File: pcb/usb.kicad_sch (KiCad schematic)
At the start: 40 parts, among them J6 USB4105-GF-A, J7 S2B-PH-SM4-TB, Q1 DMP3099L-7, Q2 DMG3418L, Q3 DMG3418L, SW1 400MSP1R6BLKM6QE, U149 SN74LVC2G132DCUR, U151 AP2112K-3.3, U152 BQ29700DSER, U153 MCP73831T-2ACI/OT

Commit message: Decrease charge indication LED brightness
- 1k current limiting resistor replaced with 4.7k
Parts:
- R283: value 1k -> 4.7k
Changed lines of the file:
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@@
 			)
 		)
-		(property "Value" "1k"
+		(property "Value" "4.7k"
 			(at 210.82 57.15 90)
 			(effects

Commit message: Add light pipe part to schematic.
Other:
- note added: "Light Pipe: PLPC3-125"
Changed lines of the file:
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@@
+		)
+	)
+	(text "Light Pipe: \nPLPC3-125"
+		(exclude_from_sim no)
+		(at 203.2 30.48 0)
+		(effects
+			(font
+				(size 1.27 1.27)
+			)
+			(href "https://www.bivar.com/parts_content/Datasheets/PLPC3-XXX.pdf")
 		)
 	)

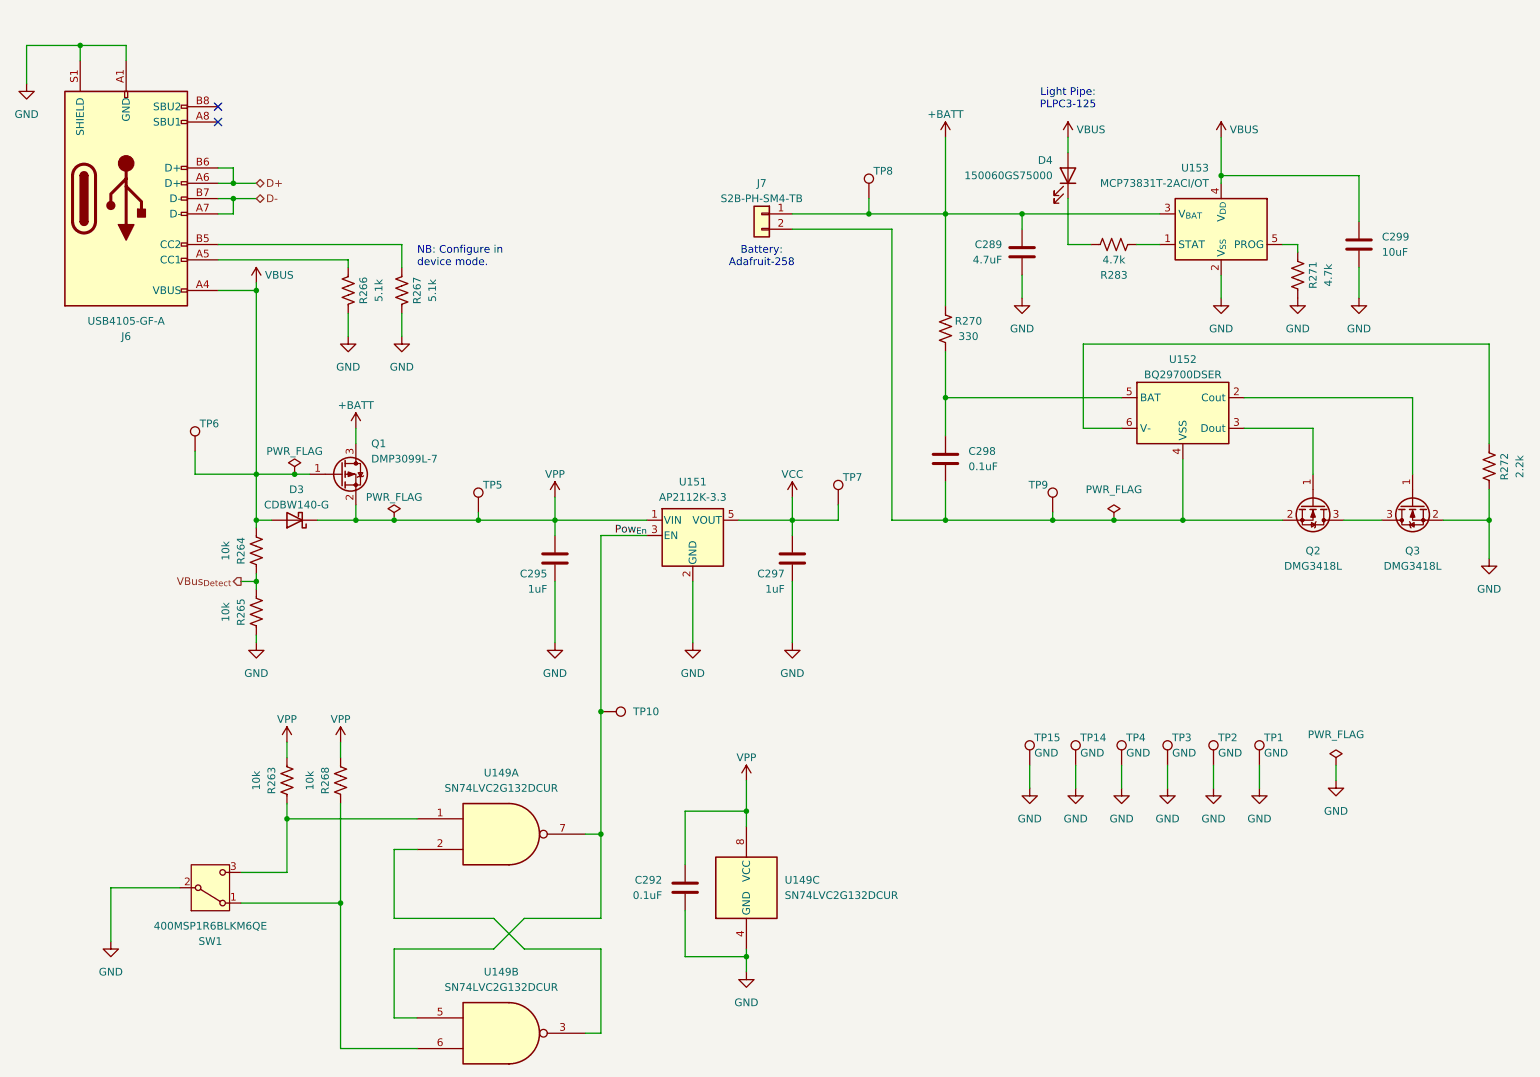
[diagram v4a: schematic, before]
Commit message: Address issues with case found during proptyping
- Add recess for reset button
- Add 3.5V power managment circuit and simplify on/off switch debounce
- Increase space in bottom porition of case for thicker battery
- Remove alignment notches from PCB -- uses features of case instead
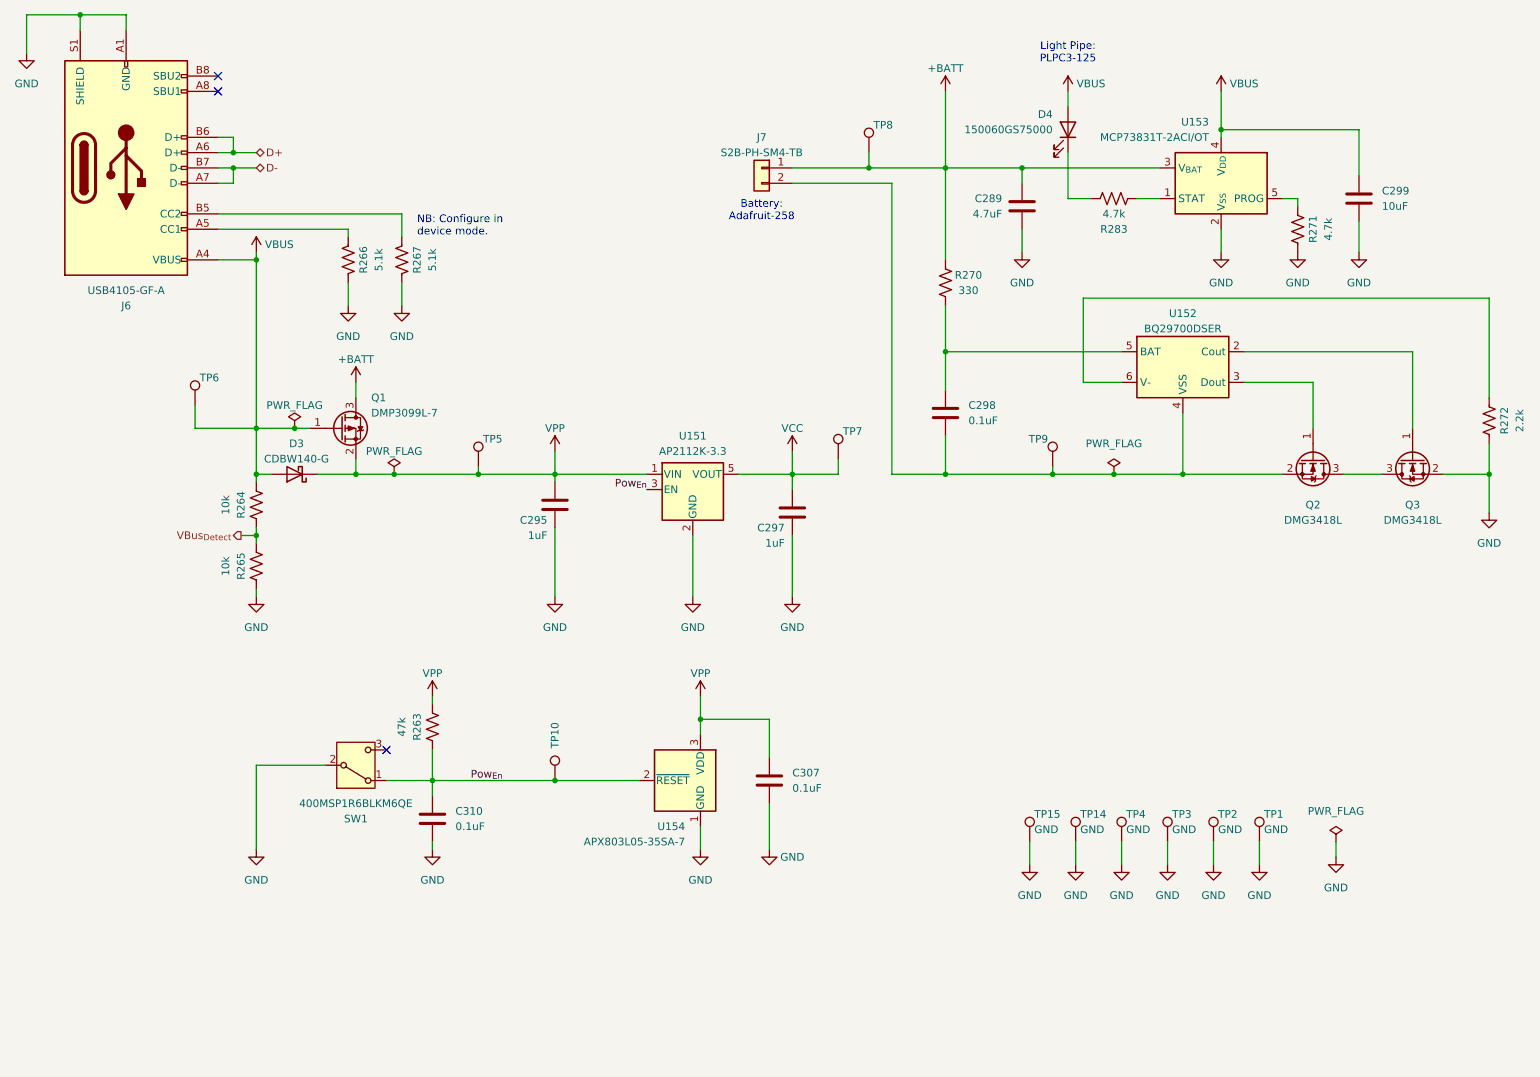
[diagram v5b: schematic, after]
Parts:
- removed C292: 0.1uF, Capacitor_SMD:C_0402_1005Metric, symbol Device:C
- removed R268: 10k, Resistor_SMD:R_0402_1005Metric, symbol Device:R_US
- removed U149: SN74LVC2G132DCUR, Package_SO:VSSOP-8_2.3x2mm_P0.5mm, symbol 74xGxx:74LVC2G00
- added C307, C310: 0.1uF, Capacitor_SMD:C_0402_1005Metric, symbol Device:C
- added U154: APX803L05-35SA-7, Package_TO_SOT_SMD:SOT-23, symbol Power_Supervisor:TPS3839DBZ
- R263: value 10k -> 47k
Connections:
- net GND: now also C307.2, C310.2, U154.1 (GND)
- net Pow_{En}: now also R263.2, SW1.1 (A), C310.1, U154.2 (~{RESET})
- net VPP: now also C307.1, U154.3 (VDD)
- net at SW1.3 (C): no longer R263.2
- no-connect marks 2 -> 3
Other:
- moved on the sheet: C289, C295, C297, C298, C299, D3, D4, J6, J7, Q1, Q2, Q3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

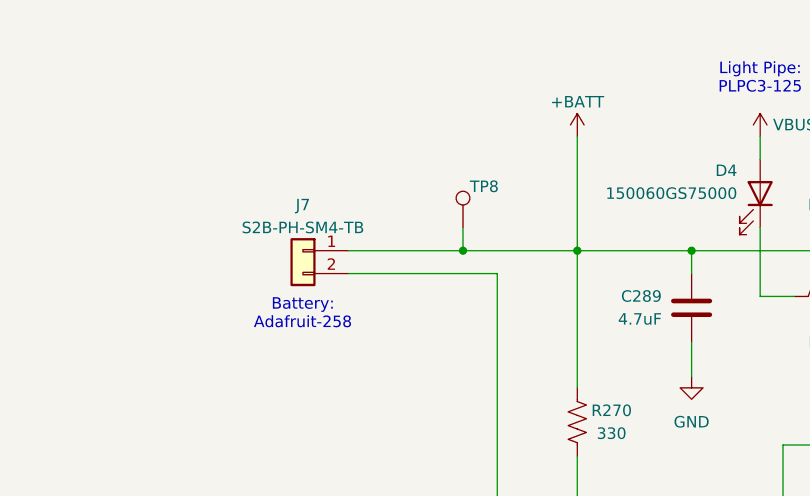
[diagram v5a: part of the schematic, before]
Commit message: Add direct wire to board option for battery
- Original connector is still there, but can be DNP for other battery
  choices.
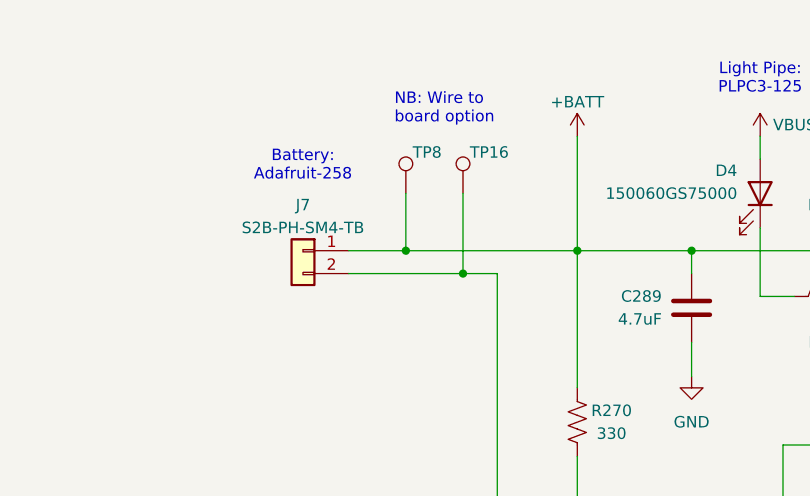
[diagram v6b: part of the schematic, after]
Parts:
- added TP16: ~, TestPoint:TestPoint_THTPad_D3.0mm_Drill1.5mm, symbol Connector:TestPoint
- TP8: value GND -> ~; footprint TestPoint:TestPoint_Pad_D2.0mm -> TestPoint:TestPoint_THTPad_D3.0mm_Drill1.5mm
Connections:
- net at C298.2, J7.2 (Pin_2), Q2.2 (S)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: now also TP16.1
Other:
- note added: "NB: Wire to board option"
- moved on the sheet: TP8
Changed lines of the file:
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@@
 		(comment 1 "Jonathan P. Newman")
 	)
+	(text "NB: Wire to\nboard option"
+		(exclude_from_sim no)
+		(at 162.56 27.94 0)
+		(effects
+			(font
+				(size 1.27 1.27)
+			)
+			(justify left bottom)
+		)
+	)
 	(text "Battery:\nAdafruit-258\n"
 		(exclude_from_sim no)
-		(at 152.4 50.8 0)
+		(at 152.4 34.29 0)
 		(effects
 			(font
@@
 	)
 	(junction
-		(at 182.88 72.39)
+		(at 163.83 41.91)
 		(diameter 0)
 		(color 0 0 0 0)
 	)
 	(junction
-		(at 68.58 102.87)
+		(at 182.88 72.39)
 		(diameter 0)
 		(color 0 0 0 0)
 	)
 	(junction
-		(at 210.82 92.71)
+		(at 68.58 102.87)
 		(diameter 0)
 		(color 0 0 0 0)
 	)
 	(junction
-		(at 157.48 92.71)
+		(at 210.82 92.71)
 		(diameter 0)
 		(color 0 0 0 0)
 	)
 	(junction
-		(at 170.18 41.91)
+		(at 157.48 92.71)
 		(diameter 0)
 		(color 0 0 0 0)
@@
 	)
 	(junction
+		(at 170.18 44.45)
+		(diameter 0)
+		(color 0 0 0 0)
+	)
+	(junction
 		(at 64.77 41.91)
 		(diameter 0)
@@
 	(wire
 		(pts
+			(xy 163.83 41.91) (xy 182.88 41.91)
+		)
+		(stroke
+			(width 0)
+			(type default)
+		)
+	)
+	(wire
+		(pts
 			(xy 212.09 153.67) (xy 212.09 157.48)
 		)
@@
 	(wire
 		(pts
-			(xy 157.48 44.45) (xy 173.99 44.45)
+			(xy 157.48 44.45) (xy 170.18 44.45)
 		)
 		(stroke
@@
 	(wire
 		(pts
+			(xy 170.18 44.45) (xy 173.99 44.45)
+		)
+		(stroke
+			(width 0)
+			(type default)
+		)
+	)
+	(wire
+		(pts
 			(xy 97.79 143.51) (xy 97.79 146.05)
 		)
@@
 	(wire
 		(pts
-			(xy 80.01 140.97) (xy 68.58 140.97)
+			(xy 170.18 35.56) (xy 170.18 44.45)
 		)
 		(stroke
@@
 	(wire
 		(pts
-			(xy 92.71 60.96) (xy 92.71 64.77)
+			(xy 80.01 140.97) (xy 68.58 140.97)
 		)
 		(stroke
@@
 	(wire
 		(pts
-			(xy 228.6 35.56) (xy 228.6 36.83)
+			(xy 92.71 60.96) (xy 92.71 64.77)
 		)
 		(stroke
@@
 	(wire
 		(pts
-			(xy 64.77 41.91) (xy 64.77 44.45)
+			(xy 228.6 35.56) (xy 228.6 36.83)
 		)
 		(stroke
@@
 	(wire
 		(pts
-			(xy 132.08 143.51) (xy 118.11 143.51)
+			(xy 64.77 41.91) (xy 64.77 44.45)
 		)
 		(stroke
@@
 	(wire
 		(pts
-			(xy 62.23 36.83) (xy 64.77 36.83)
+			(xy 132.08 143.51) (xy 118.11 143.51)
 		)
 		(stroke
@@
 	(wire
 		(pts
-			(xy 46.99 16.51) (xy 39.37 16.51)
+			(xy 62.23 36.83) (xy 64.77 36.83)
 		)
 		(stroke
@@
 	(wire
 		(pts
-			(xy 273.05 92.71) (xy 265.43 92.71)
+			(xy 46.99 16.51) (xy 39.37 16.51)
 		)
 		(stroke
@@
 	(wire
 		(pts
-			(xy 170.18 41.91) (xy 182.88 41.91)
+			(xy 273.05 92.71) (xy 265.43 92.71)
 		)
 		(stroke
@@
 	(wire
 		(pts
-			(xy 157.48 41.91) (xy 170.18 41.91)
+			(xy 157.48 41.91) (xy 163.83 41.91)
 		)
 		(stroke
@@
 	(wire
 		(pts
-			(xy 170.18 39.37) (xy 170.18 41.91)
+			(xy 163.83 35.56) (xy 163.83 41.91)
 		)
 		(stroke
@@
 	(symbol
 		(lib_id "Connector:TestPoint")
-		(at 170.18 39.37 0)
+		(at 163.83 35.56 0)
 		(unit 1)
 		(exclude_from_sim no)
@@
 		(dnp no)
 		(property "Reference" "TP8"
-			(at 170.942 34.798 0)
+			(at 164.592 30.988 0)
 			(effects
 				(font
@@
 			)
 		)
-		(property "Value" "GND"
-			(at 170.942 37.338 0)
+		(property "Value" "~"
+			(at 164.592 33.528 0)
 			(effects
 				(font
@@
 			)
 		)
-		(property "Footprint" "TestPoint:TestPoint_Pad_D2.0mm"
-			(at 175.26 39.37 0)
+		(property "Footprint" "TestPoint:TestPoint_THTPad_D3.0mm_Drill1.5mm"
+			(at 168.91 35.56 0)
 			(effects
 				(font
@@
 		)
 		(property "Datasheet" "~"
-			(at 175.26 39.37 0)
+			(at 168.91 35.56 0)
 			(effects
 				(font
@@
 		)
 		(property "Description" "test point"
-			(at 170.18 39.37 0)
+			(at 163.83 35.56 0)
 			(effects
 				(font
@@
 		)
 		(property "Voltage" ""
-			(at 170.18 39.37 0)
+			(at 163.83 35.56 0)
 			(effects
 				(font
@@
 		)
 		(property "Datasheet1" ""
-			(at 170.18 39.37 0)
+			(at 163.83 35.56 0)
 			(effects
 				(font
@@
 		)
 		(property "Part No." ""
-			(at 170.18 39.37 0)
+			(at 163.83 35.56 0)
 			(effects
 				(font
@@
 		)
 		(property "Tolerance" ""
-			(at 170.18 39.37 0)
+			(at 163.83 35.56 0)
 			(effects
 				(font
@@
 					(unit 1)
 				)
+			)
+		)
+	)
+	(symbol
+		(lib_id "Connector:TestPoint")
+		(at 170.18 35.56 0)
+		(unit 1)
+		(exclude_from_sim no)
+		(in_bom yes)
+		(on_board yes)
+		(dnp no)
+		(property "Reference" "TP16"
+			(at 170.942 30.988 0)
+			(effects
+				(font
+					(size 1.27 1.27)
+				)
+				(justify left)
+			)
+		)
+		(property "Value" "~"
+			(at 170.942 33.528 0)
+			(effects
+				(font
+					(size 1.27 1.27)
+				)
+				(justify left)
+				(hide yes)
+			)
+		)
+		(property "Footprint" "TestPoint:TestPoint_THTPad_D3.0mm_Drill1.5mm"
+			(at 175.26 35.56 0)
+			(effects
+				(font
+					(size 1.27 1.27)
+				)
+				(hide yes)
+			)
+		)
+		(property "Datasheet" "~"
+			(at 175.26 35.56 0)
+			(effects
+				(font
+					(size 1.27 1.27)
+				)
+				(hide yes)
+			)
+		)
+		(property "Description" "test point"
+			(at 170.18 35.56 0)
+			(effects
+				(font
+					(size 1.27 1.27)
+				)
+				(hide yes)
+			)
+		)
+		(property "Voltage" ""
+			(at 170.18 35.56 0)
+			(effects
+				(font
+					(size 1.27 1.27)
+				)
+				(hide yes)
+			)
+		)
+		(property "Datasheet1" ""
+			(at 170.18 35.56 0)
+			(effects
+				(font
+					(size 1.27 1.27)
+				)
+				(hide yes)
+			)
+		)
+		(property "Part No." ""
+			(at 170.18 35.56 0)
+			(effects
+				(font
+					(size 1.27 1.27)
+				)
+				(hide yes)
+			)
+		)
+		(property "Tolerance" ""
+			(at 170.18 35.56 0)
+			(effects
+				(font
+					(size 1.27 1.27)
+				)
+			)
+		)
+		(pin "1"
+		)
+		(instances
+			(project "ephys-test-board"
+				(path "/ffaa6ffd-73fa-4da3-9ff1-78fa7369281f/3204537c-edba-465e-8dbf-7f75aa43b711"
+					(reference "TP16")
+					(unit 1)
+				)

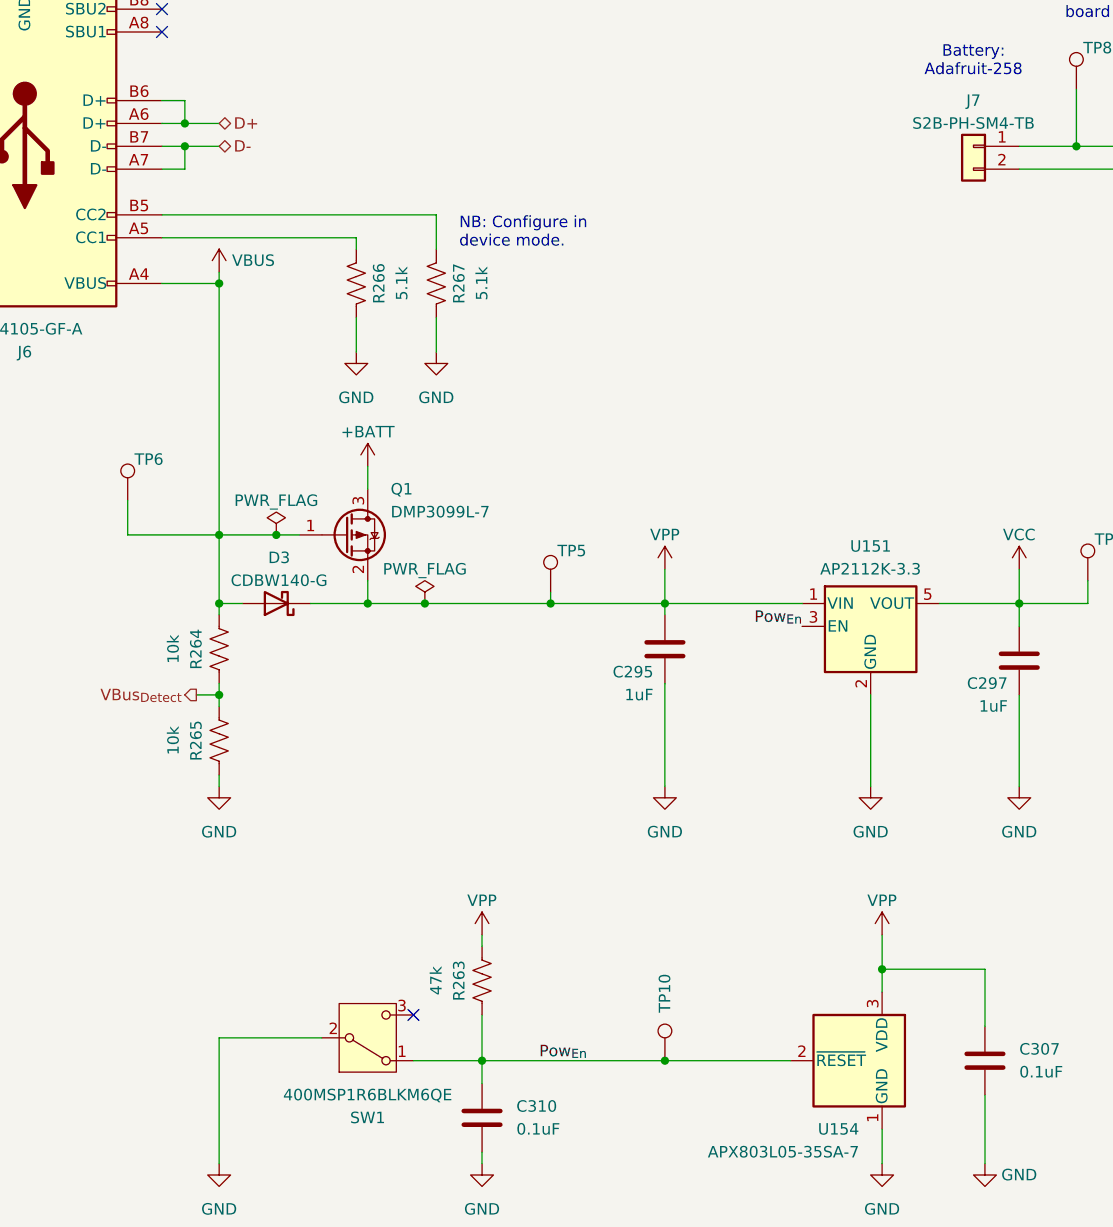
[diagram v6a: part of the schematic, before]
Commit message: Add protention diode to USB input
- Same part that has been verified on stimjim-hv
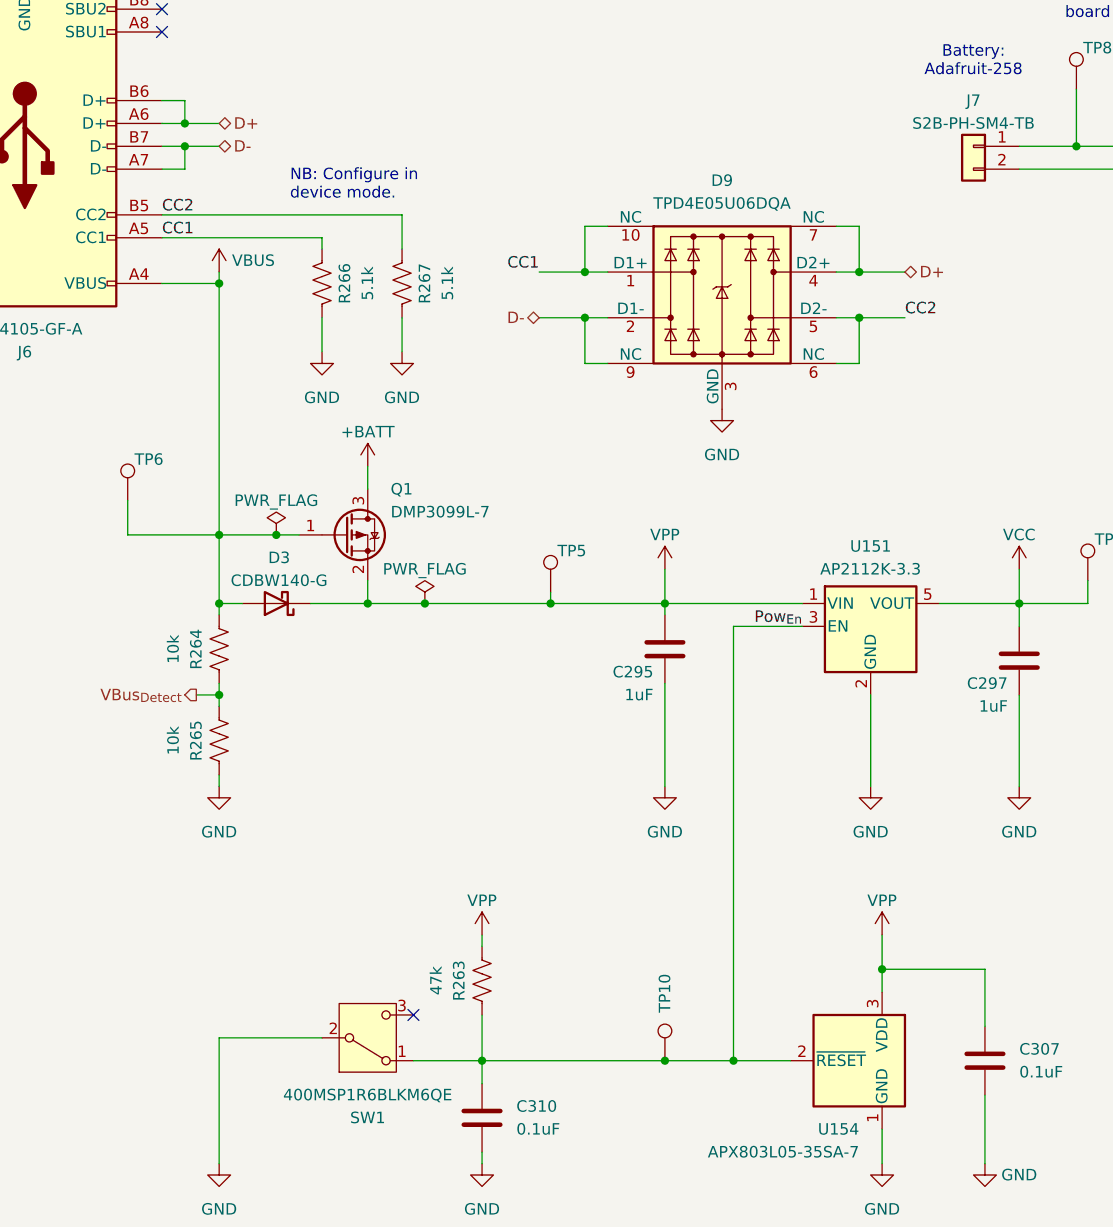
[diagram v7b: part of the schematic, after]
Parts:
- added D9: TPD4E05U06DQA, Package_SON:USON-10_2.5x1.0mm_P0.5mm, symbol Power_Protection:TPD4E05U06DQA
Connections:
- net D+: now also D9.4 (D2+), D9.7 (NC)
- net D-: now also D9.2 (D1-), D9.9 (NC)
- net GND: now also D9.3 (GND), D9.8 (GND)
- net CC1: now reaches J6.A5 (CC1), R266.1
- net CC1: now also D9.1 (D1+), D9.10 (NC)
- net CC2: now reaches J6.B5 (CC2), R267.1
- net CC2: now also D9.5 (D2-), D9.6 (NC)
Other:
- moved on the sheet: R266, R267
